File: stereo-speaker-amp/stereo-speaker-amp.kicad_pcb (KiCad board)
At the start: 2 copper layers, 50.6 x 54.6 mm, 30 parts, among them J1 PWR IN, J2 SPK 1, J3 SPK 2, J4 AUX IN, U1 TDA2822

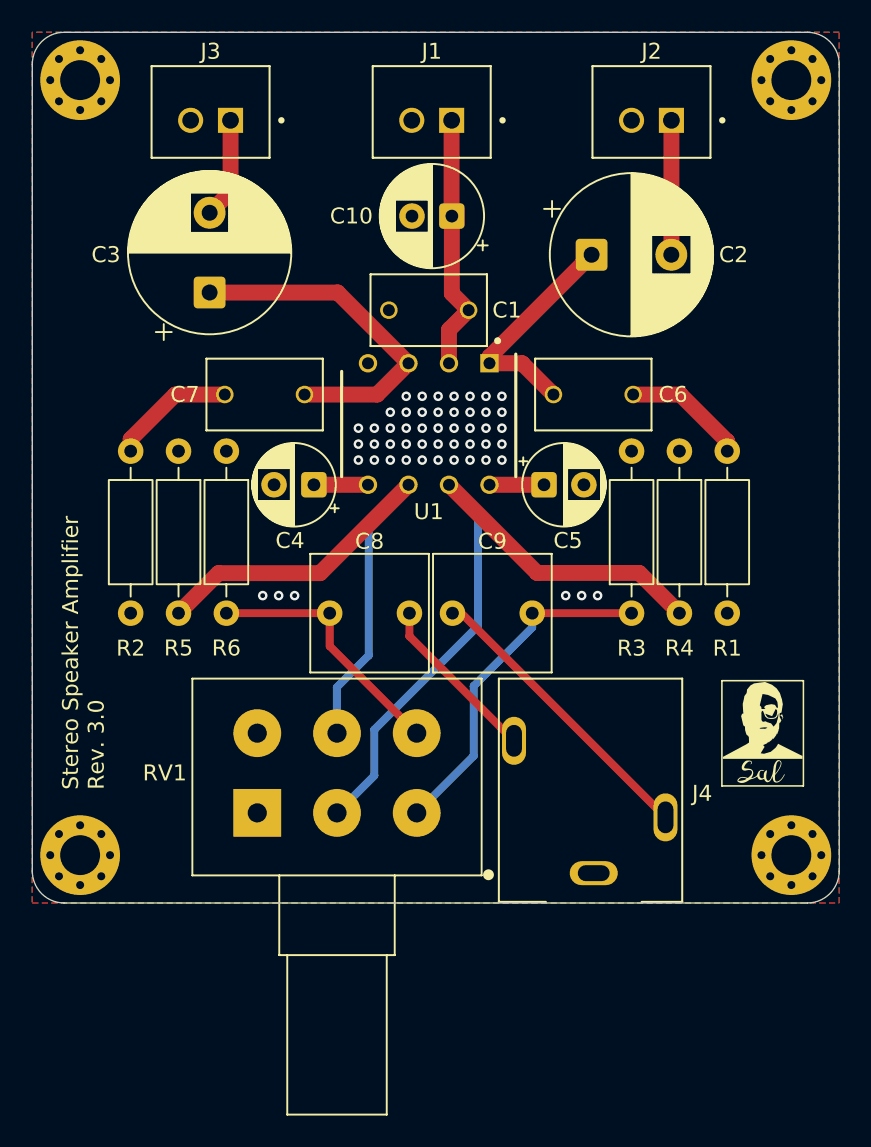
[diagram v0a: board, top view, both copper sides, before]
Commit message: Migrate stereo-speaker-amp to KiCad 10 and add self-contained symbol, footprint, and 3D model libraries
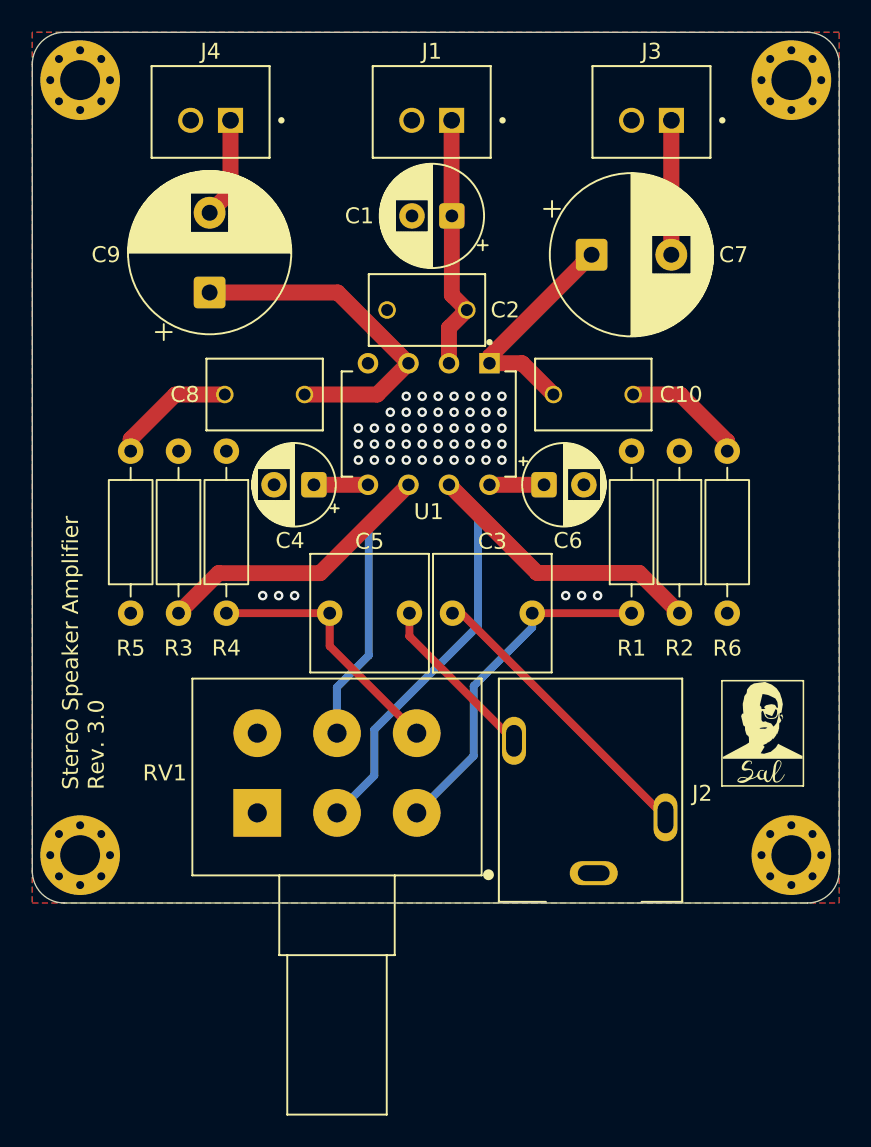
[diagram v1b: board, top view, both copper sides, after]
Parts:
- U1: footprint footprints:DIP762W55P254L1092H332Q8N -> footprints:DIP762W45P254L1092H508Q8
- moved C2 0.11 mm to (145.3, 84.6)
- renumbered C10 to C1, C6 to C10, C1 to C2, C9 to C3, C8 to C5, C5 to C6, C2 to C7, C7 to C8, C3 to C9, J4 to J2, J2 to J3, J3 to J4, R3 to R1, R4 to R2, R5 to R3, R6 to R4, R2 to R5, R1 to R6
